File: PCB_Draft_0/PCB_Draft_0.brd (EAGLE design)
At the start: 160 x 100 mm, 7 parts, among them IC1 ADS7828, IC2 PCA9534PW

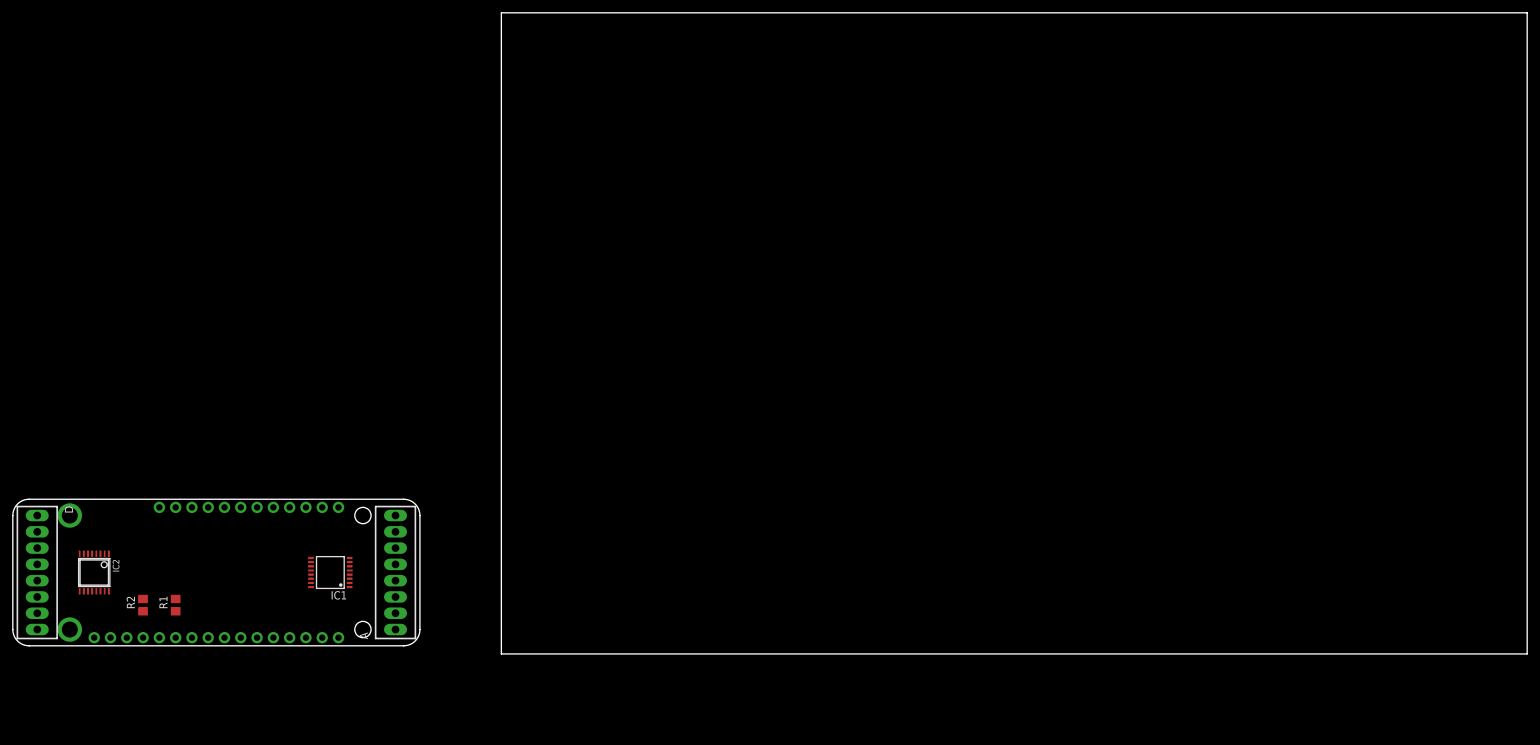
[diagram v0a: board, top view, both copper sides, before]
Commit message: Added I2C Headers
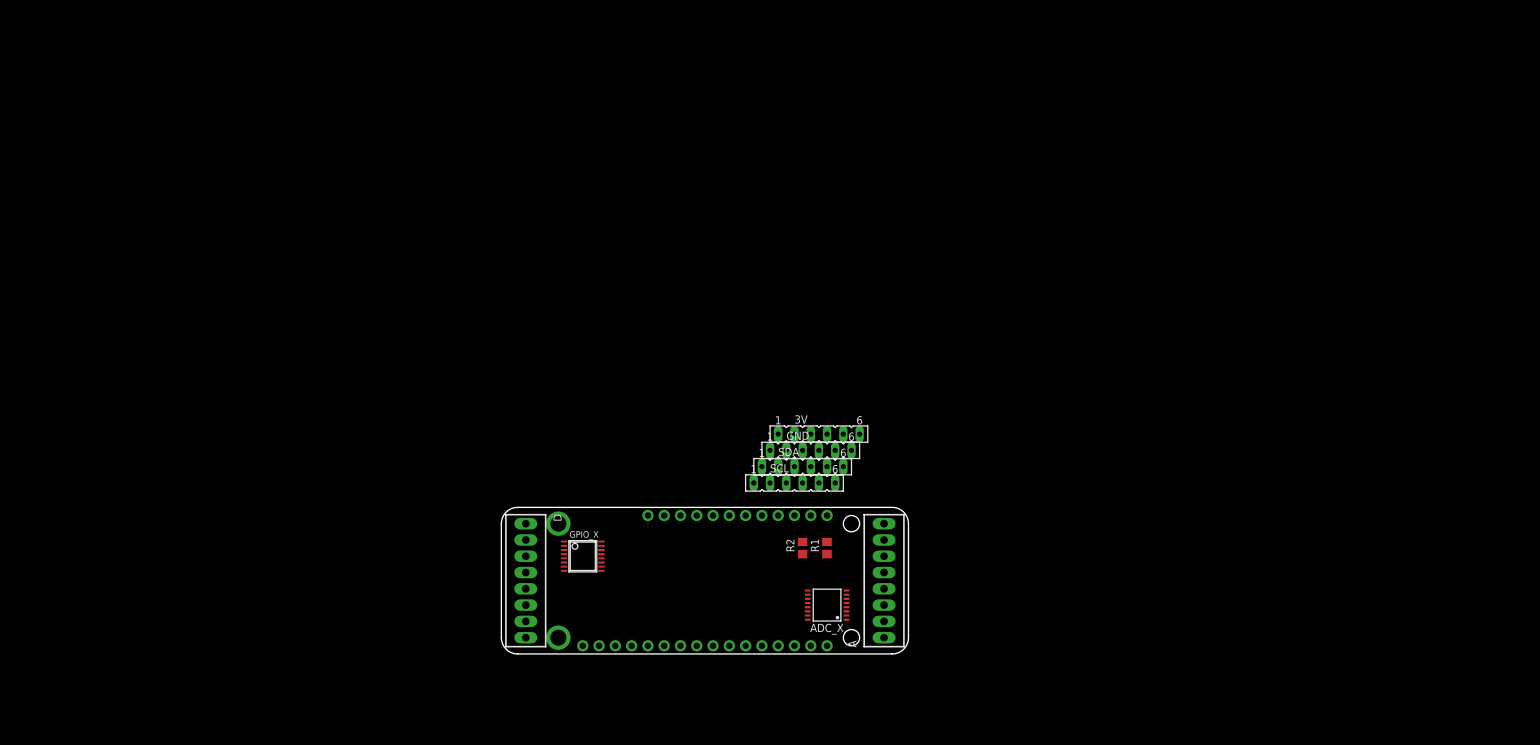
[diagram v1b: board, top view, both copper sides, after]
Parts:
- removed IC1: ADS7828, burr-brown:TSSOP16-PW
- removed IC2: PCA9534PW, micro-philips:TSSOP16
- added 3V, GND, SCL, SDA: (no value), con-lsta:FE06
- added ADC_X: ADS7828, burr-brown:TSSOP16-PW
- added GPIO_X: PCA9534PW, micro-philips:TSSOP16
- moved R2 103.3 mm to (47.0, 16.5)
- moved R1 102.0 mm to (50.8, 16.5)
- moved A 76.2 mm to (59.7, 11.4)
- moved D 76.2 mm to (3.81, 11.4)
- moved MS1 76.2 mm to (6.35, 0.00)
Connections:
- net 3V: now also 3V.1, 3V.2, 3V.3, 3V.4, 3V.5, 3V.6, ADC_X.16, GPIO_X.16; no longer IC1.16, IC2.16
- net GND: now also ADC_X.9, GND.1, GND.2, GND.3, GND.4, GND.5, GND.6; no longer IC1.9
- net N$1: now also GPIO_X.4; no longer IC2.4
- net N$10: now also ADC_X.2; no longer IC1.2
- net N$11: now also ADC_X.3; no longer IC1.3
- net N$12: now also ADC_X.4; no longer IC1.4
- net N$13: now also ADC_X.5; no longer IC1.5
- net N$14: now also ADC_X.6; no longer IC1.6
- net N$15: now also ADC_X.7; no longer IC1.7
- net N$16: now also ADC_X.8; no longer IC1.8
- net N$2: now also GPIO_X.5; no longer IC2.5
- net N$3: now also GPIO_X.6; no longer IC2.6
- net N$4: now also GPIO_X.7; no longer IC2.7
- net N$5: now also GPIO_X.9; no longer IC2.9
- net N$6: now also GPIO_X.10; no longer IC2.10
- net N$7: now also GPIO_X.11; no longer IC2.11
- net N$8: now also GPIO_X.12; no longer IC2.12
- net N$9: now also ADC_X.1; no longer IC1.1
- net SCL: now also ADC_X.14, GPIO_X.14, SCL.1, SCL.2, SCL.3, SCL.4, SCL.5, SCL.6; no longer IC1.14, IC2.14
- net SDA: now also ADC_X.15, GPIO_X.15, SDA.1, SDA.2, SDA.3, SDA.4, SDA.5, SDA.6; no longer IC1.15, IC2.15
- net VSS: now also GPIO_X.8; no longer IC2.8
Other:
- board size 160 x 100 mm -> 63.5 x 22.9 mm

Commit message: SomeStuff
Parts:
- removed 3V, GND, SCL, SDA: (no value), con-lsta:FE06
- added A_COM: (no value), ME507:3POL254
- added C1: 5u, rcl:C0805
- added I2C: (no value), con-lstb:MA04-1
- added R3: 0, rcl:M0805
- moved GPIO_X 7.62 mm to (12.7, 7.62)
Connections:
- removed net VSS: GPIO_X.8
- new net A_COM: ADC_X.11, A_COM.3, C1.2, R3.1
- new net INT: GPIO_X.13, MS1.19
- new net N$17: ADC_X.10, C1.1
- net 3V: now also A_COM.1, I2C.1; no longer 3V.1, 3V.2, 3V.3, 3V.4, 3V.5, 3V.6
- net GND: now also ADC_X.12, ADC_X.13, A_COM.2, GPIO_X.1, GPIO_X.2, GPIO_X.3, GPIO_X.8, I2C.4, R3.2; no longer GND.1, GND.2, GND.3, GND.4, GND.5, GND.6
- net SCL: now also I2C.3; no longer SCL.1, SCL.2, SCL.3, SCL.4, SCL.5, SCL.6
- net SDA: now also I2C.2; no longer SDA.1, SDA.2, SDA.3, SDA.4, SDA.5, SDA.6

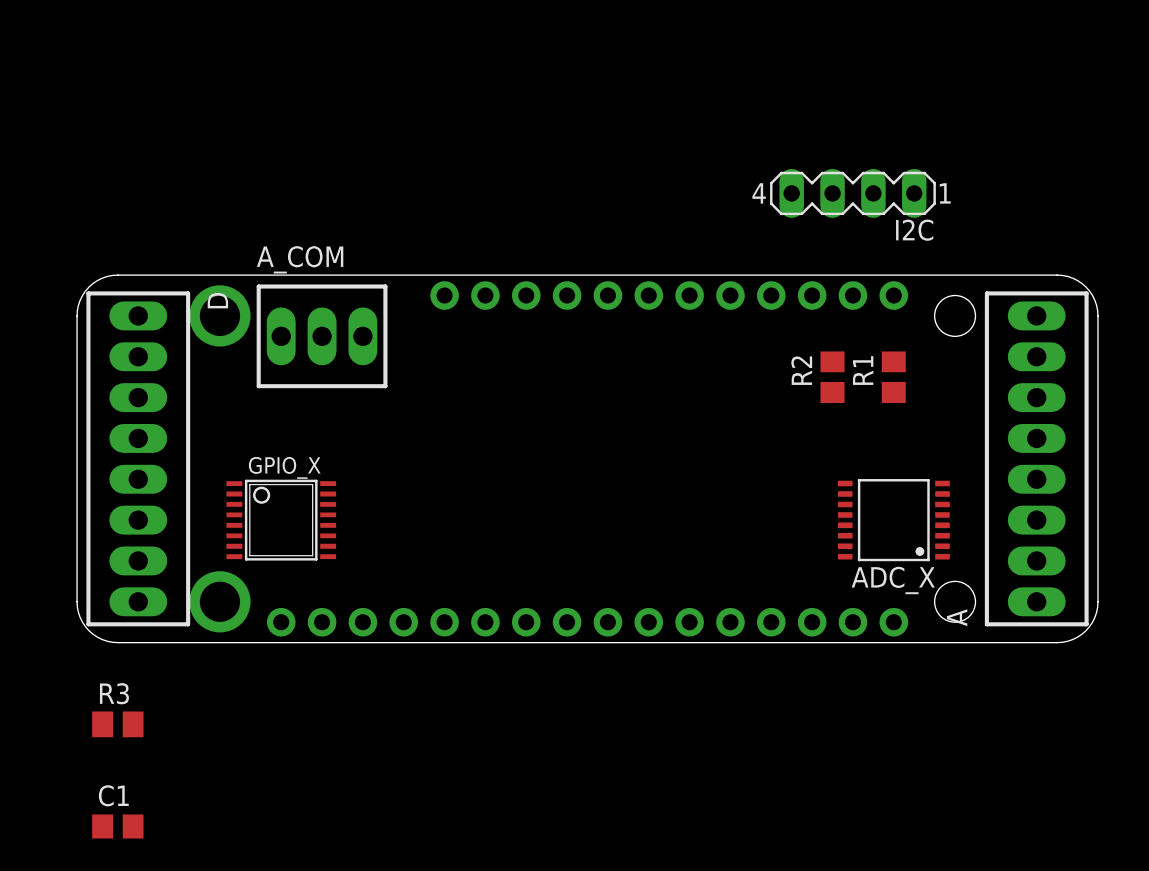
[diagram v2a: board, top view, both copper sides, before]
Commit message: Expanded board, reorganized stuff, added motor driver
Submitted to canvas
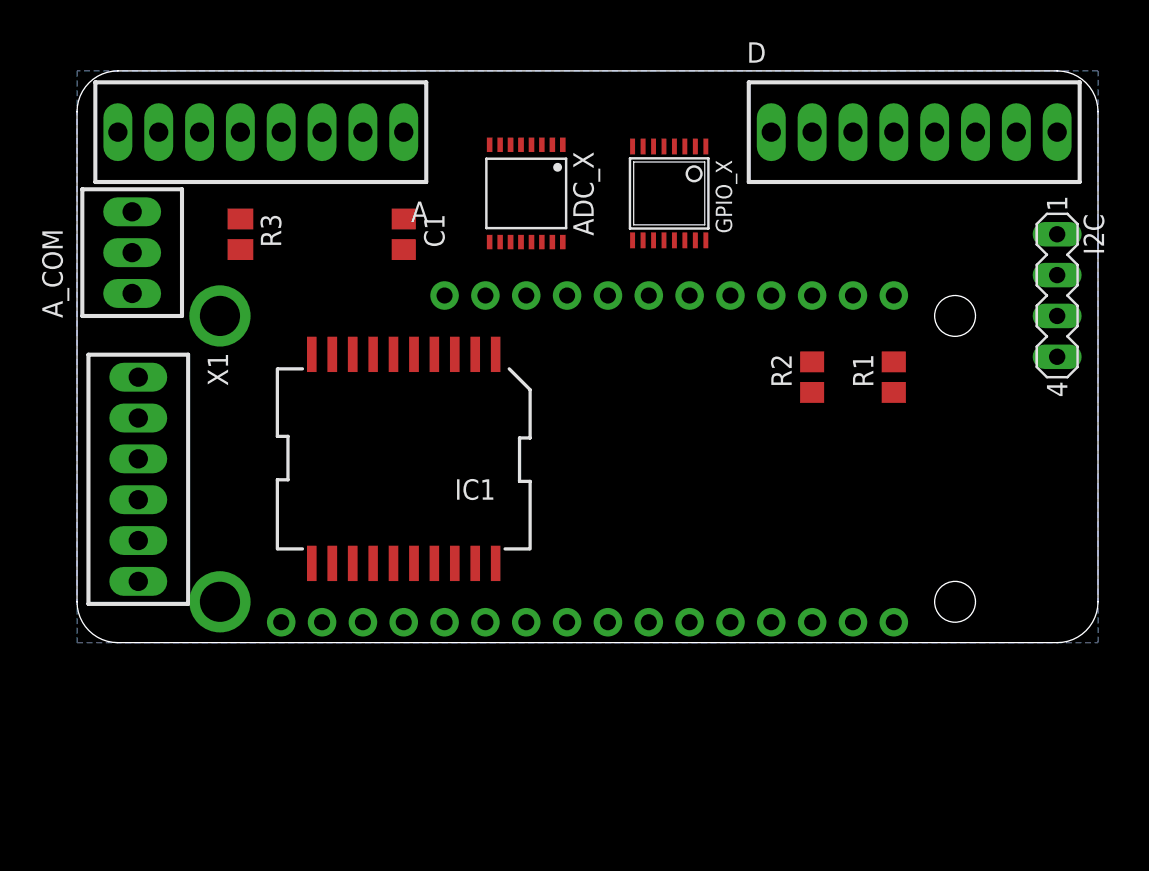
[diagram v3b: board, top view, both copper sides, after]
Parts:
- added IC1: L6205PD, st-microelectronics:POWERSO-20
- added X1: (no value), ME507:6POL254
- moved A 52.4 mm to (11.4, 31.8), turned to 180 degrees
- moved D 52.4 mm to (52.1, 31.8), turned to 0 degrees
- moved C1 40.9 mm to (20.3, 25.4), turned to 270 degrees
- moved GPIO_X 31.5 mm to (36.8, 27.9), turned to 180 degrees
- moved R3 31.4 mm to (10.2, 25.4), turned to 270 degrees
- moved ADC_X 30.6 mm to (27.9, 27.9), turned to 180 degrees
- moved I2C 14.2 mm to (61.0, 21.6), turned to 270 degrees
- moved A_COM 12.9 mm to (3.43, 24.3), turned to 90 degrees
- moved R2 1.27 mm to (45.7, 16.5)
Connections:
- new net N$18: IC1.9, X1.3
- new net N$19: IC1.3, X1.4
- new net N$20: IC1.12, X1.5
- new net N$21: IC1.18, X1.6
- new net N$22: IC1.6, MS1.23
- new net N$24: IC1.15, MS1.20
- new net N$25: IC1.14, MS1.21
- new net N$26: IC1.7, MS1.22
- new net VBOOT: IC1.17
- new net VCP: IC1.4
- new net V_MOT: IC1.19, IC1.2, X1.1
- net GND: now also IC1.1, IC1.10, IC1.11, IC1.13, IC1.20, IC1.8, X1.2
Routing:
- added copper zone on layer 16, net GND
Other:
- board size 63.5 x 22.9 mm -> 63.5 x 35.6 mm

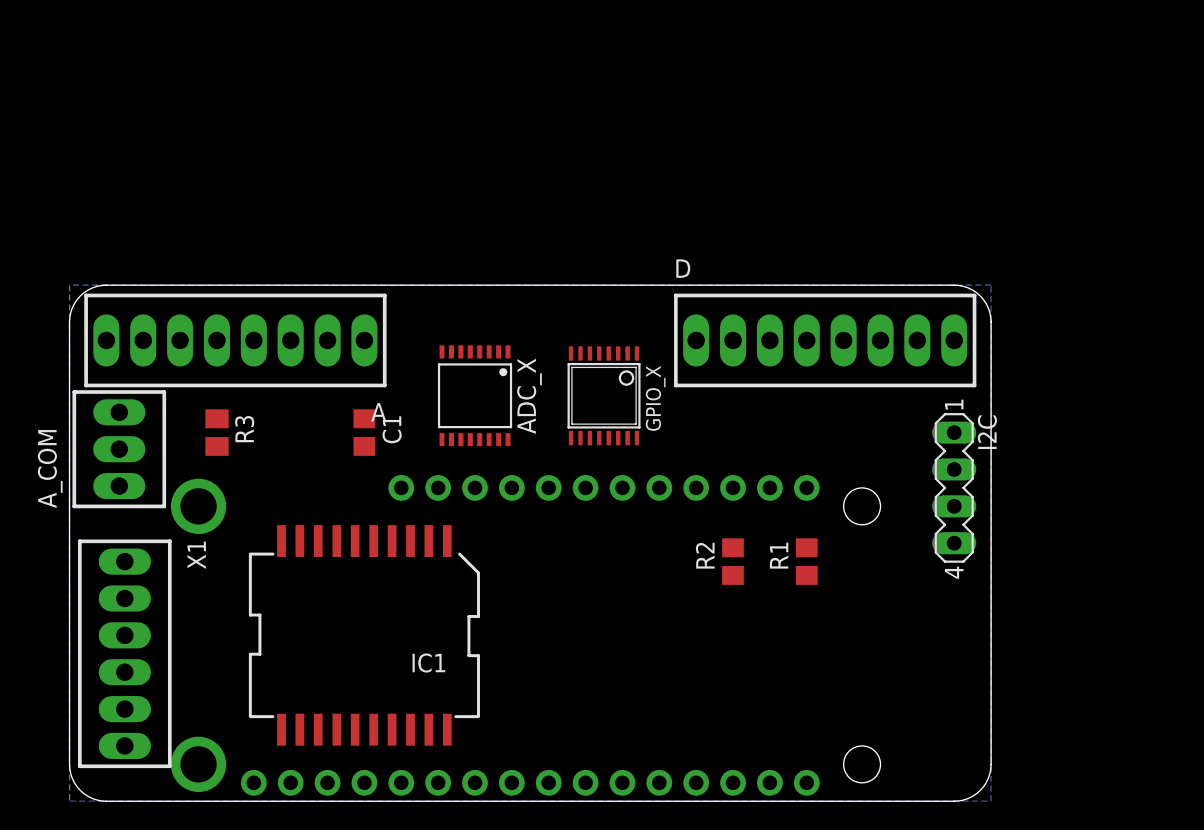
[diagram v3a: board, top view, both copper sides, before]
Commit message: Restarted schematic on larger sheet format. Added second motor driver
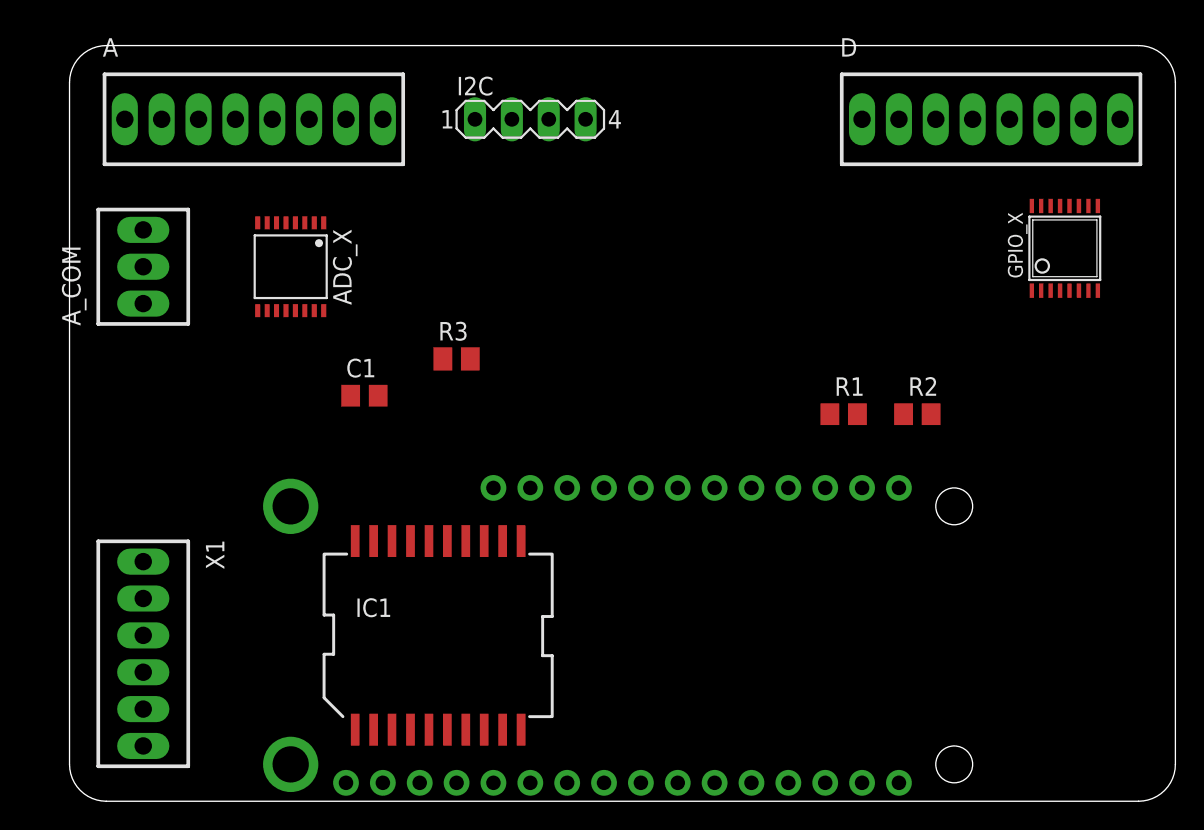
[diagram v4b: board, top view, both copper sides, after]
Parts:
- moved I2C 38.7 mm to (31.8, 47.0), turned to 0 degrees
- moved GPIO_X 33.3 mm to (68.6, 38.1), turned to 0 degrees
- moved D 19.1 mm to (63.5, 47.0)
- moved R3 17.3 mm to (26.7, 30.5), turned to 0 degrees
- moved R2 16.3 mm to (58.4, 26.7), turned to 0 degrees
- moved ADC_X 15.5 mm to (15.2, 36.8)
- moved A 15.3 mm to (12.7, 47.0), turned to 0 degrees
- moved A_COM 12.7 mm to (5.08, 36.8)
- moved R1 10.5 mm to (53.3, 26.7), turned to 0 degrees
- moved MS1 6.35 mm to (12.7, 0.00)
- moved IC1 5.08 mm to (25.4, 11.4), turned to 0 degrees
- moved C1 2.54 mm to (20.3, 27.9), turned to 0 degrees
- moved X1 1.27 mm to (5.08, 10.2)
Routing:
- removed copper zone on layer 16, net GND
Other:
- board size 63.5 x 35.6 mm -> 76.2 x 52.1 mm
